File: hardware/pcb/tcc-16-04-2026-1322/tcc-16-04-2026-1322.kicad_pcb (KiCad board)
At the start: 2 copper layers, 145.5 x 145.5 mm, 81 parts, among them J2 Conn_02x20_Odd_Even, SW1 SW_Push, SW10 SW_Push, SW11 SW_Push, SW12 SW_Push, SW13 SW_Push, SW14 SW_Push, SW15 SW_Push, SW16 SW_Push, SW17 SW_Push, SW18 SW_Push, SW19 SW_Push, SW2 SW_Push, SW20 SW_Push, SW21 SW_Push, SW22 SW_Push, SW23 SW_Push, SW24 SW_Push, SW25 SW_Push, SW26 SW_Push, SW27 SW_Push, SW28 SW_Push, SW29 SW_Push, SW3 SW_Push, SW30 SW_Push, SW31 SW_Push, SW32 SW_Push, SW33 SW_Push, SW34 SW_Push, SW35 SW_Push, SW36 SW_Push, SW37 SW_Push, SW38 SW_Push, SW4 SW_Push, SW5 SW_Push, SW6 SW_Push, SW7 SW_Push, SW8 SW_Push, SW9 SW_Push

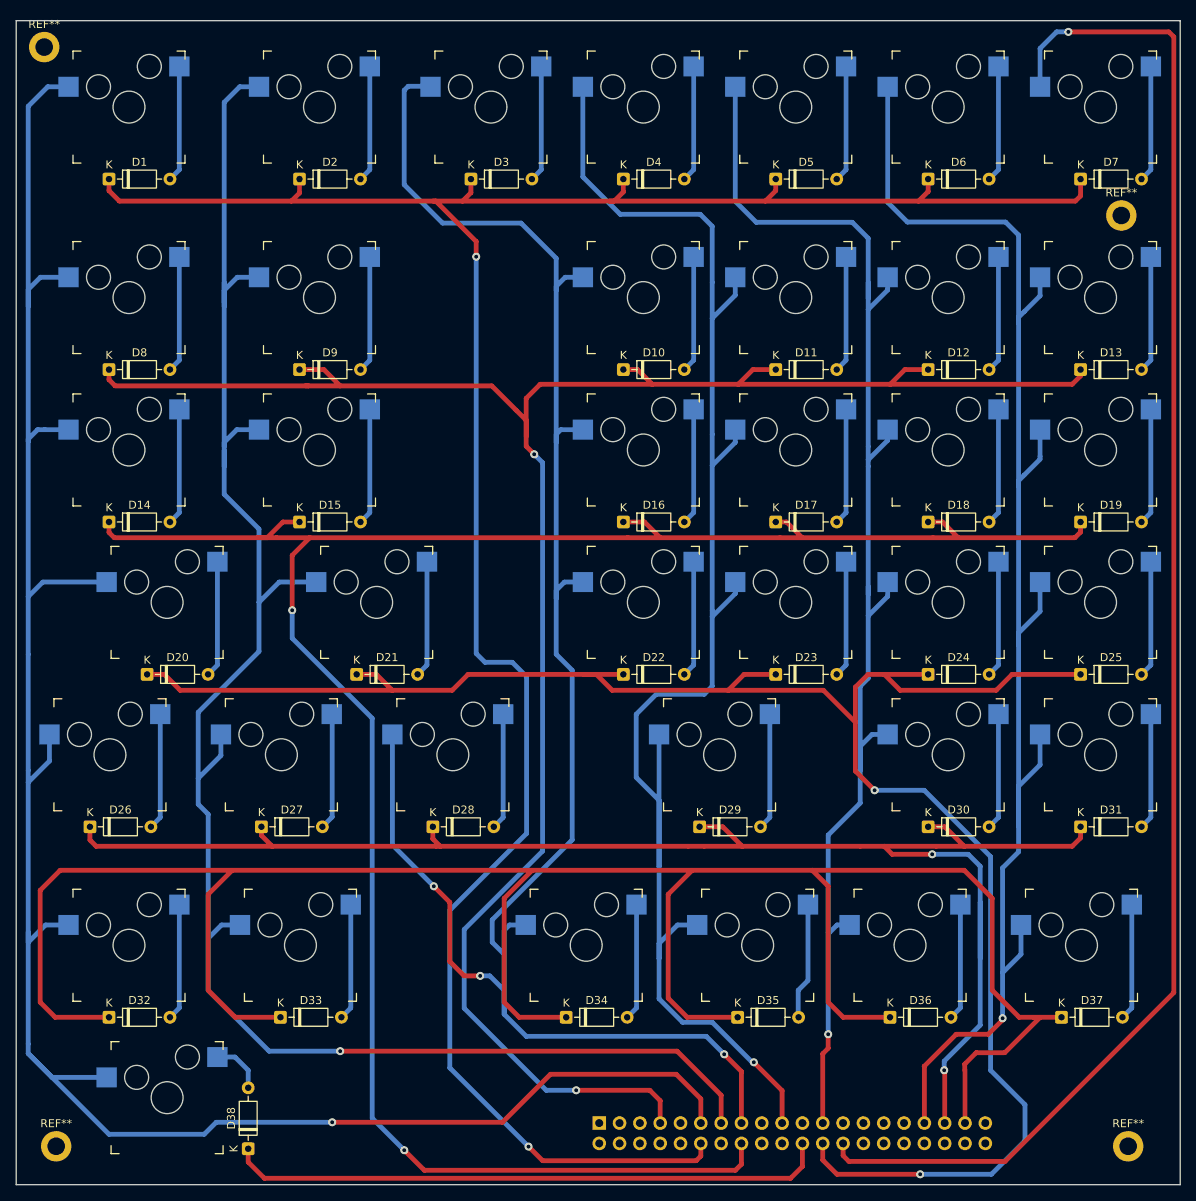
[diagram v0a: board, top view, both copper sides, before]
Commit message: update pcb artifacts and refresh project scaffolding/docs
Includes latest KiCad board/project changes, generated PCB PDF exports, and repository housekeeping updates across docs and software/hardware placeholder structure.

Made-with: Cursor
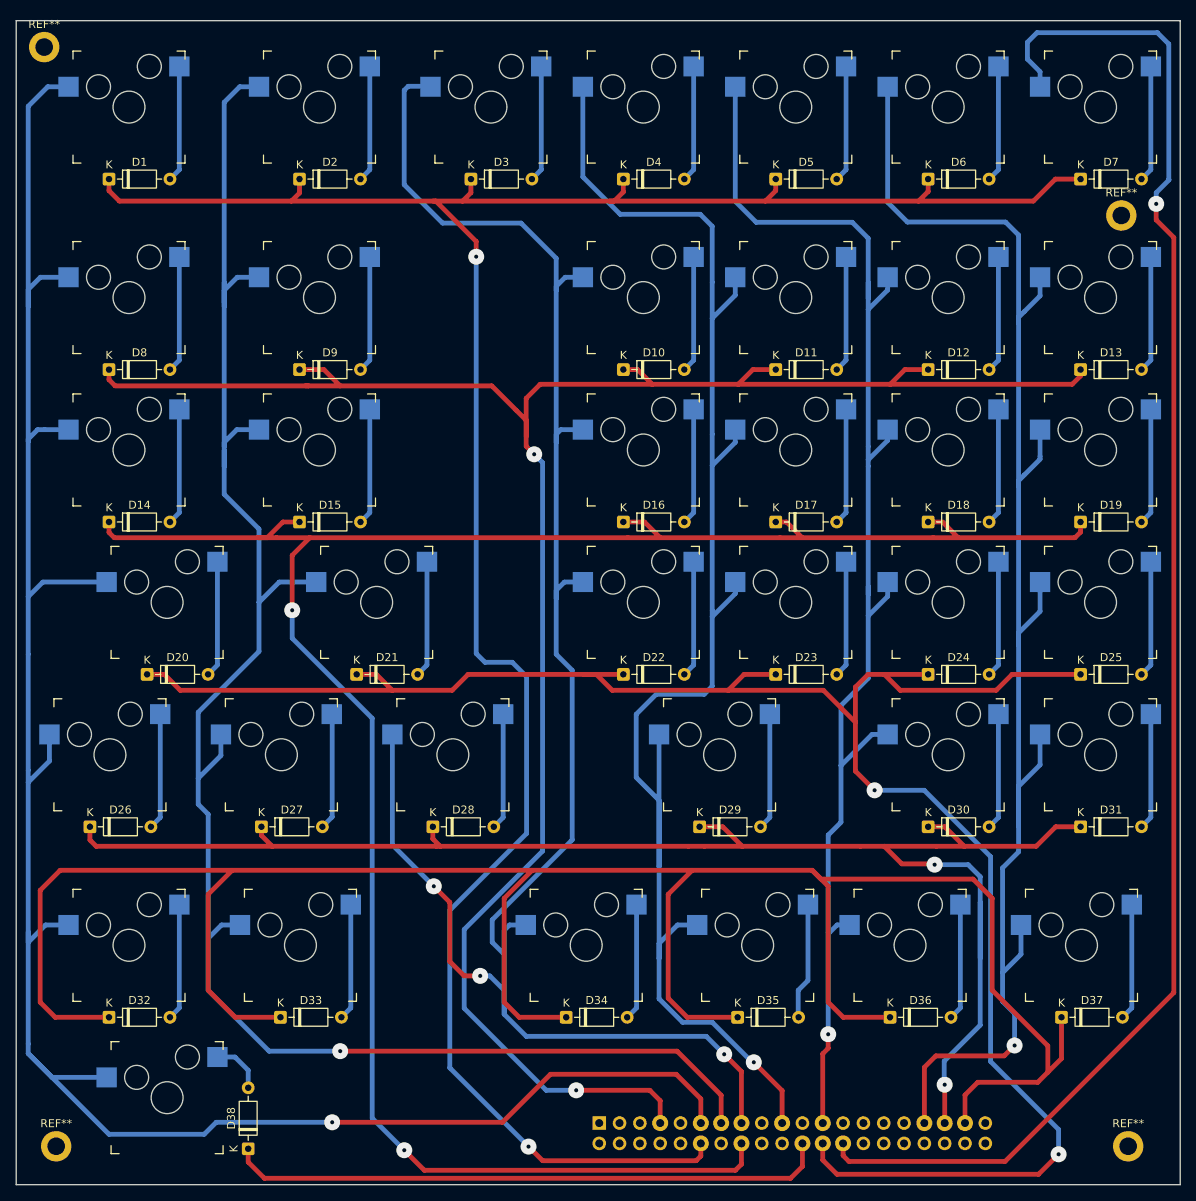
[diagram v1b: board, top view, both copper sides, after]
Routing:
- net Row3: track 244.5 -> 251.4 mm
- net Row5: track 291.7 -> 298.2 mm
- net Col5: track 194.3 -> 198.2 mm
- net Col6: track 194.0 -> 197.0 mm
- net Row4: track 199.3 -> 197.7 mm
- net Row0: track 299.8 -> 298.6 mm
